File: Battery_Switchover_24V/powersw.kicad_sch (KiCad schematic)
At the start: 57 parts, among them J10 ATX_2X3, J11 ATX_2X3, J12 ATX_2X3, J13 ATX_2X3, J2 M8, J4 M8, J5 M8, J8 ATX_2X3, J9 ATX_2X3, Q10 FDBL86066-F085, Q4 FDBL86066-F085, Q5 FDBL86066-F085, Q6 FDBL86066-F085, Q7 FDBL86066-F085, Q8 FDBL86066-F085, Q9 FDBL86066-F085, U16 LM74610QDGKRQ1, U3 IRS20752, U6 LM74610QDGKRQ1, U7 IRS20752, U9 IRS20752

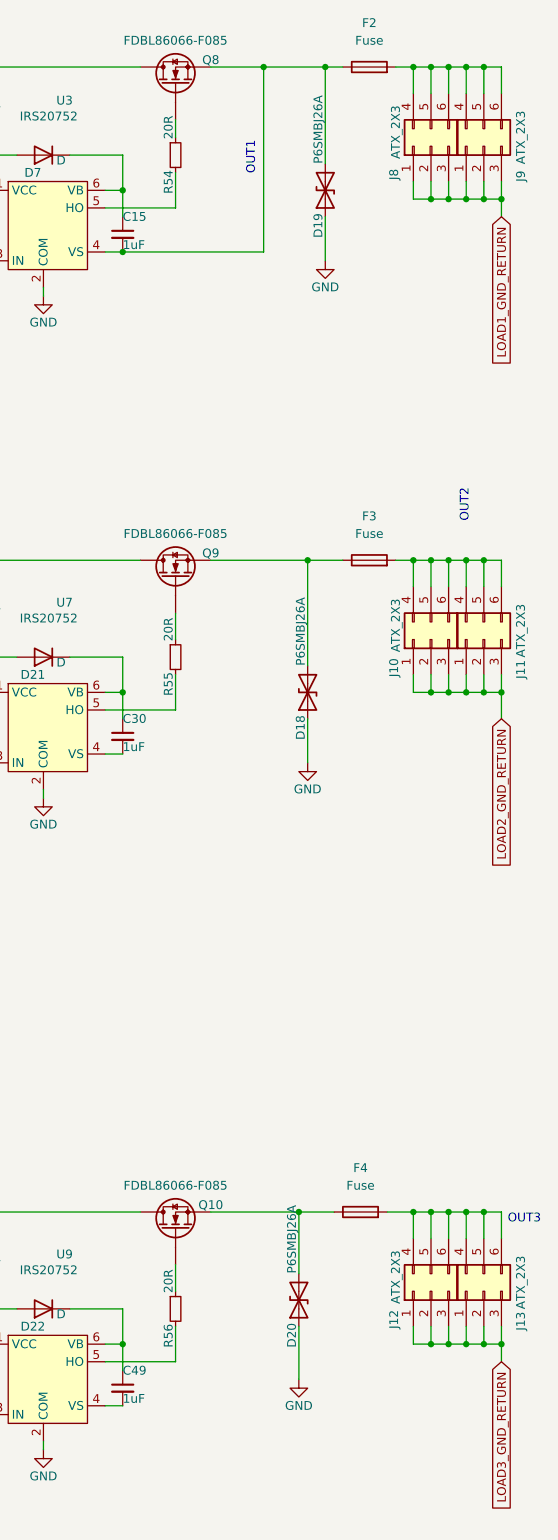
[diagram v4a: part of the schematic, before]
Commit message: fuse placement
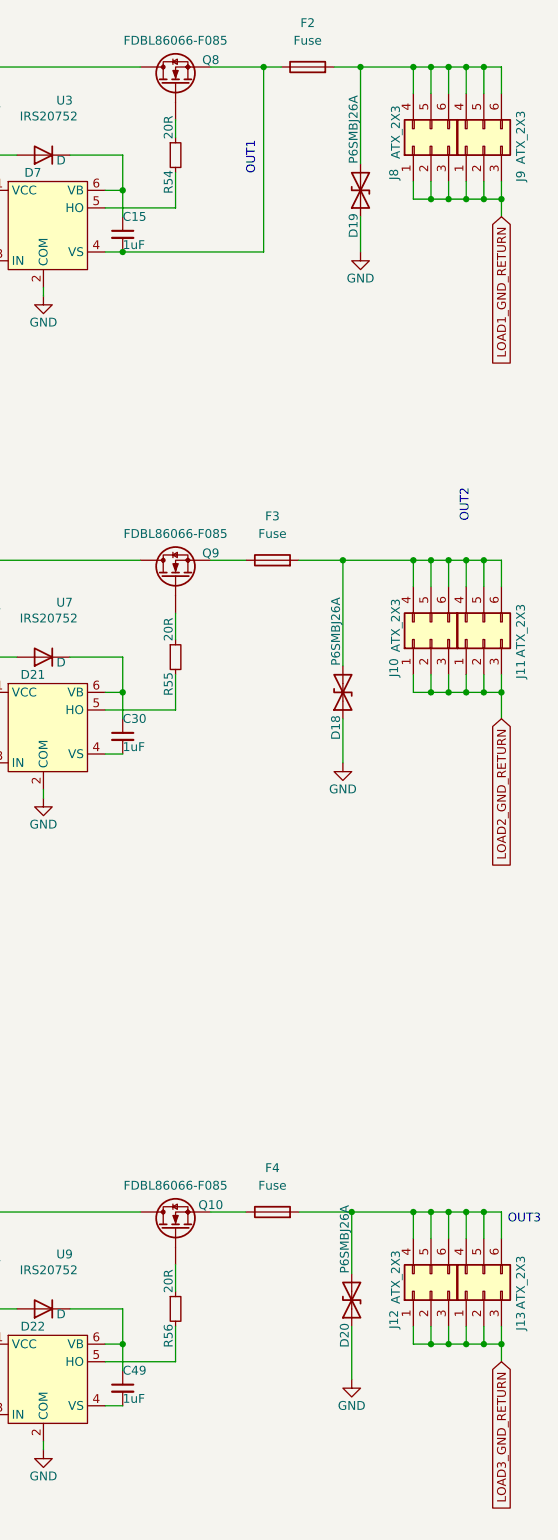
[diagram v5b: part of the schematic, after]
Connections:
- net at C15.2, F2.1, Q8.2 (S)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: no longer D19.2 (A2)
- net at F4.1, Q10.2 (S): no longer D20.2 (A2)
- net at F2.2, J8.4 (Pin_4), J8.5 (Pin_5)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: now also D19.2 (A2)
- net at F3.1, Q9.2 (S): no longer D18.2 (A2)
- net at F4.2, J12.4 (Pin_4), J12.5 (Pin_5)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: now also D20.2 (A2)
- net at F3.2, J10.4 (Pin_4), J10.5 (Pin_5)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: now also D18.2 (A2)
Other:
- moved on the sheet: D18, D19, D20, F2, F3, F4

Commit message: minor changes
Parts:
- added Q1, Q12, Q15: BC817, Package_TO_SOT_SMD:SOT-23, symbol Transistor_BJT:BC817
- added R67, R68, R69: 4K7, Resistor_SMD:R_0603_1608Metric, symbol Device:R_Small
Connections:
- net EMERGENCY_STOP: now also R67.1, R68.1, R69.1
- net GND: now also Q1.2 (E), Q12.2 (E), Q15.2 (E)
- net at U3.3 (IN): now also R64.2, Q1.3 (C)
- net at U7.3 (IN): now also R65.2, Q12.3 (C)
- net at U9.3 (IN): now also R66.2, Q15.3 (C)
- new net: Q1.1 (B), R67.2
- new net: Q15.1 (B), R69.2
- new net: Q12.1 (B), R68.2
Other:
- moved on the sheet: R64

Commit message: Routing
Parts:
- removed C12, C8: 2.2uf, Capacitor_SMD:C_0805_2012Metric, symbol Device:C_Small_US
- removed U16, U6: LM74610QDGKRQ1, Package_SO:VSSOP-8_3x3mm_P0.65mm, symbol LM74610QDGKRQ1:LM74610QDGKRQ1
- added C8, C83: 100nF 50V X7R, Capacitor_SMD:C_0805_2012Metric, symbol Device:C_Small
- added U19, U8: AP74700Q, Package_TO_SOT_SMD:SOT-23-6, symbol AP74700Q:AP74700Q
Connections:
- net GND: now also U19.2 (GND), U8.2 (GND)
- net VBATT: now also C83.1, U8.6 (ANODE)
- net VIN: now also C8.1, U19.6 (ANODE)
- net VOUT: now also U19.4 (CATHODE), U8.4 (CATHODE)
- net at F4.1, Q10.2 (S): now also C49.2, U9.4 (VS)
- net at C30.2, U7.4 (VS): now also F3.1, Q9.2 (S)
- net at Q6.1 (G), Q7.1 (G): now also U19.5 (GATE)
- net at Q4.1 (G), Q5.1 (G): now also U8.5 (GATE)
- new net: C8.2, U19.1 (VCP)
- new net: C83.2, U8.1 (VCP)
- new net BATT_EN: U8.3 (EN)
- new net MAINS_EN: U19.3 (EN)

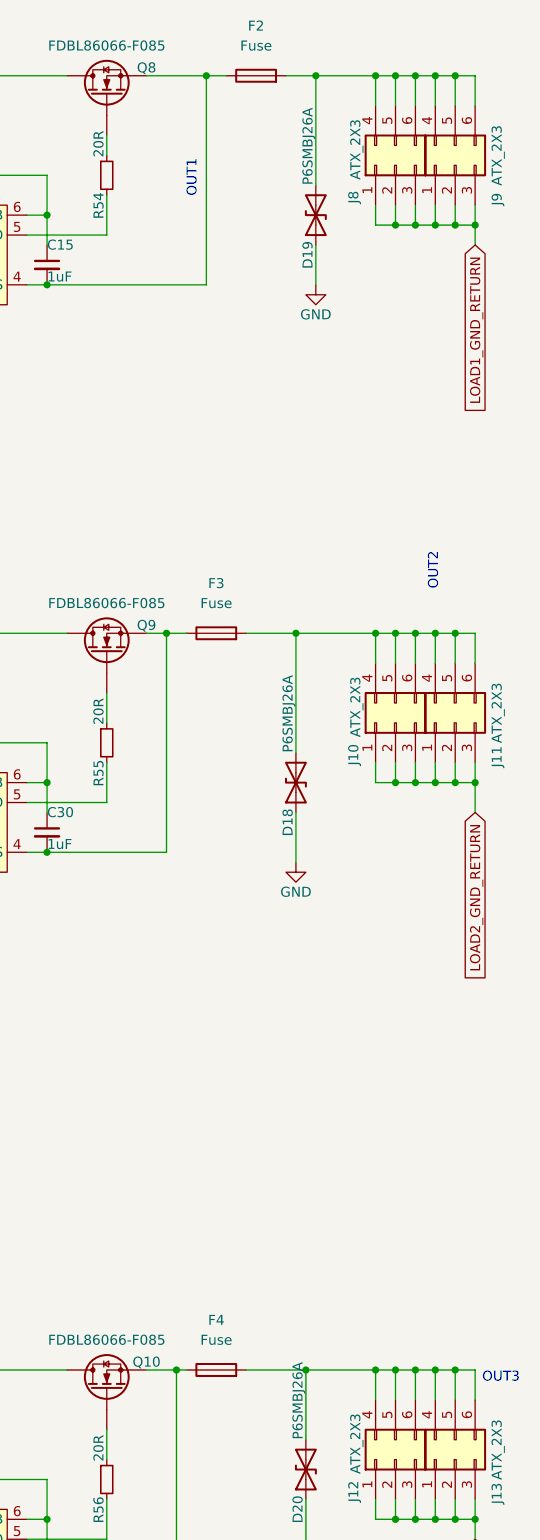
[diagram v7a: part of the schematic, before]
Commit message: Via stitching
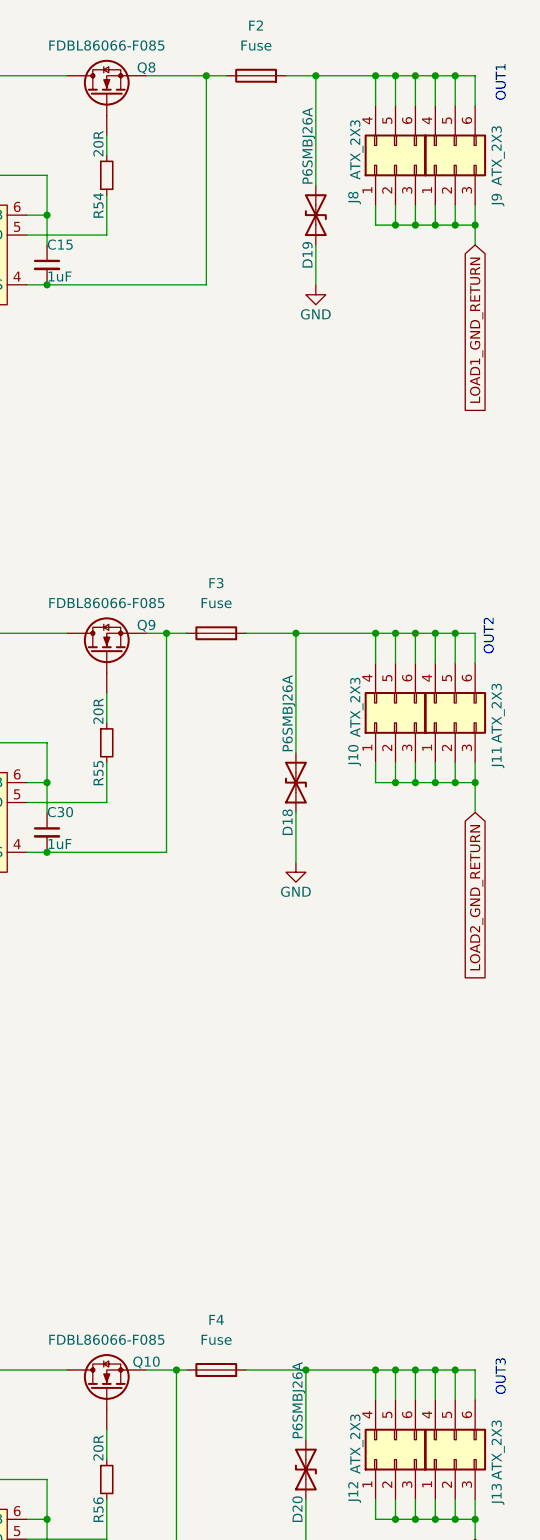
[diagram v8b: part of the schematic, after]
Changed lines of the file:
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@@
 	(text "OUT2"
 		(exclude_from_sim no)
-		(at 379.476 97.536 90)
+		(at 386.588 105.918 90)
 		(effects
 			(font
@@
 	(text "OUT1"
 		(exclude_from_sim no)
-		(at 348.6785 47.4345 90)
+		(at 388.112 35.306 90)
 		(effects
 			(font
@@
 	(text "OUT3"
 		(exclude_from_sim no)
-		(at 388.112 200.406 0)
+		(at 388.112 200.406 90)
 		(effects
 			(font
